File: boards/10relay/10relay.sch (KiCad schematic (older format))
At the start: 0 parts

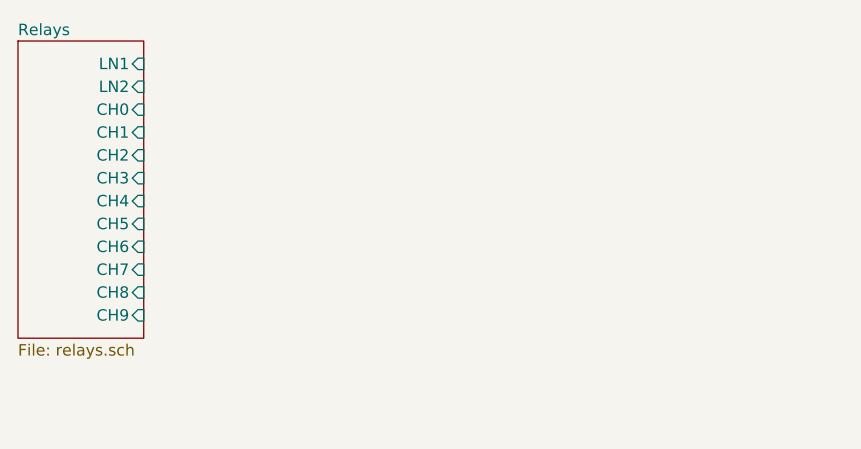
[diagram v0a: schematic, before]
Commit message: Added relay sheet and power sheet
The relay sheet has been added to simplify viewing. It
contains all the relays for all 10 channels. Power sheet
for everything power related such as logic level conversion
and regulators.
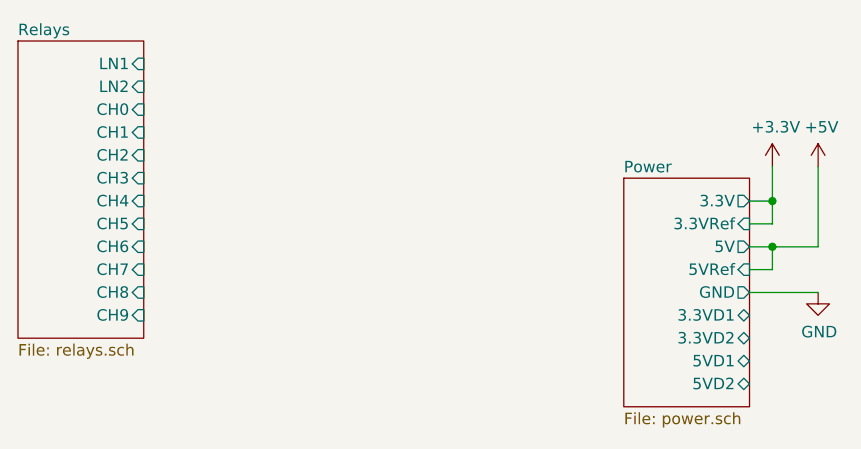
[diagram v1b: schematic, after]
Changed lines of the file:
@@
 $Descr A4 11693 8268
 encoding utf-8
-Sheet 1 2
+Sheet 1 3
 Title "10relay"
-Date "2020-11-21"
+Date "2020-11-22"
 Rev "1"
 Comp "Sidings Media"
@@
 F13 "CH9" I R 1550 2400 50
 $EndSheet
+$Comp
+L power:+3.3V #PWR0101
+U 1 1 5FD67CC1
+P 4300 1750
+F 0 "#PWR0101" H 4300 1600 50  0001 C CNN
+F 1 "+3.3V" H 4315 1923 50  0000 C CNN
+F 2 "" H 4300 1750 50  0001 C CNN
+F 3 "" H 4300 1750 50  0001 C CNN
+	1    4300 1750
+	1    0    0    -1
+$EndComp
+$Comp
+L power:+5V #PWR0102
+U 1 1 5FD6867D
+P 4500 1750
+F 0 "#PWR0102" H 4500 1600 50  0001 C CNN
+F 1 "+5V" H 4515 1923 50  0000 C CNN
+F 2 "" H 4500 1750 50  0001 C CNN
+F 3 "" H 4500 1750 50  0001 C CNN
+	1    4500 1750
+	1    0    0    -1
+$EndComp
+Wire Wire Line
+	4300 1750 4300 1900
+Wire Wire Line
+	4300 1900 4200 1900
+$Comp
+L power:GND #PWR0103
+U 1 1 5FD6943F
+P 4500 2300
+F 0 "#PWR0103" H 4500 2050 50  0001 C CNN
+F 1 "GND" H 4505 2127 50  0000 C CNN
+F 2 "" H 4500 2300 50  0001 C CNN
+F 3 "" H 4500 2300 50  0001 C CNN
+	1    4500 2300
+	1    0    0    -1
+$EndComp
+$Sheet
+S 3650 1800 550  1000
+U 5FD671B9
+F0 "Power" 50
+F1 "power.sch" 50
+F2 "3.3V" O R 4200 1900 50
+F3 "5V" O R 4200 2100 50
+F4 "GND" O R 4200 2300 50
+F5 "3.3VD1" B R 4200 2400 50
+F6 "3.3VD2" B R 4200 2500 50
+F7 "5VD1" B R 4200 2600 50
+F8 "5VD2" B R 4200 2700 50
+F9 "3.3VRef" I R 4200 2000 50
+F10 "5VRef" I R 4200 2200 50
+$EndSheet
+Wire Wire Line
+	4200 2000 4300 2000
+Wire Wire Line
+	4300 2000 4300 1900
+Connection ~ 4300 1900
+Wire Wire Line
+	4200 2100 4300 2100
+Wire Wire Line
+	4500 2100 4500 1750
+Wire Wire Line
+	4200 2200 4300 2200
+Wire Wire Line
+	4300 2200 4300 2100
+Connection ~ 4300 2100
+Wire Wire Line
+	4300 2100 4500 2100
+Wire Wire Line
+	4200 2300 4500 2300
 $EndSCHEMATC
